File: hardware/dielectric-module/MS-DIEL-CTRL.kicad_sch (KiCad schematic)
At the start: 54 parts, among them J1 24V_IN, J2 CAN, J3 FLUSH_SOL, J4 PUMP_CHILL_DEION, J5 ANALOG_SENSORS, J6 TEMP_1WIRE, J7 FLOW_FLOATS, J8 PROG_USB, Q1 AO3400A, Q2 AO3400A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

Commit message: hw(dielectric): human-readable schematic engine (power glyphs, stubbed labels, blocks, NC, PWR_FLAG, title); add missing MCP2518FD crystal; ERC 0 errors
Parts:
- added C11, C12: 18pF, Capacitor_SMD:C_0805_2012Metric, symbol Device:C
- added Y1: 40MHz, Crystal:Crystal_SMD_3215-2Pin_3.2x1.5mm, symbol Device:Crystal
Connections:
- net GND: now also C11.2, C12.2
- net OSC1: now also C11.1, Y1.1
- net OSC2: now also C12.1, Y1.2
- no-connect marks 0 -> 20
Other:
- note added: "ANALOG + DIGITAL SENSORS"
- note added: "CAN-FD: MCP2518FD + TJA1051 xcvr"
- note added: "ESP32-S3 MCU + PROGRAM / USB HEADER"
- note added: "FLUSH SOLENOID DRIVERS (low-side N-FET)"
- note added: "POWER: 24V in -> 5V buck -> 3V3 LDO"
- note added: "PUMP / CHILLER / DEIONISER (SSR drive)"
- company: (none) -> Microspark
- title: (none) -> MS-DIEL-CTRL  Dielectric / Coolant CAN-FD Controller
- moved on the sheet: C1, C10, C2, C3, C4, C5, C6, C7, C8, C9, D1, D2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

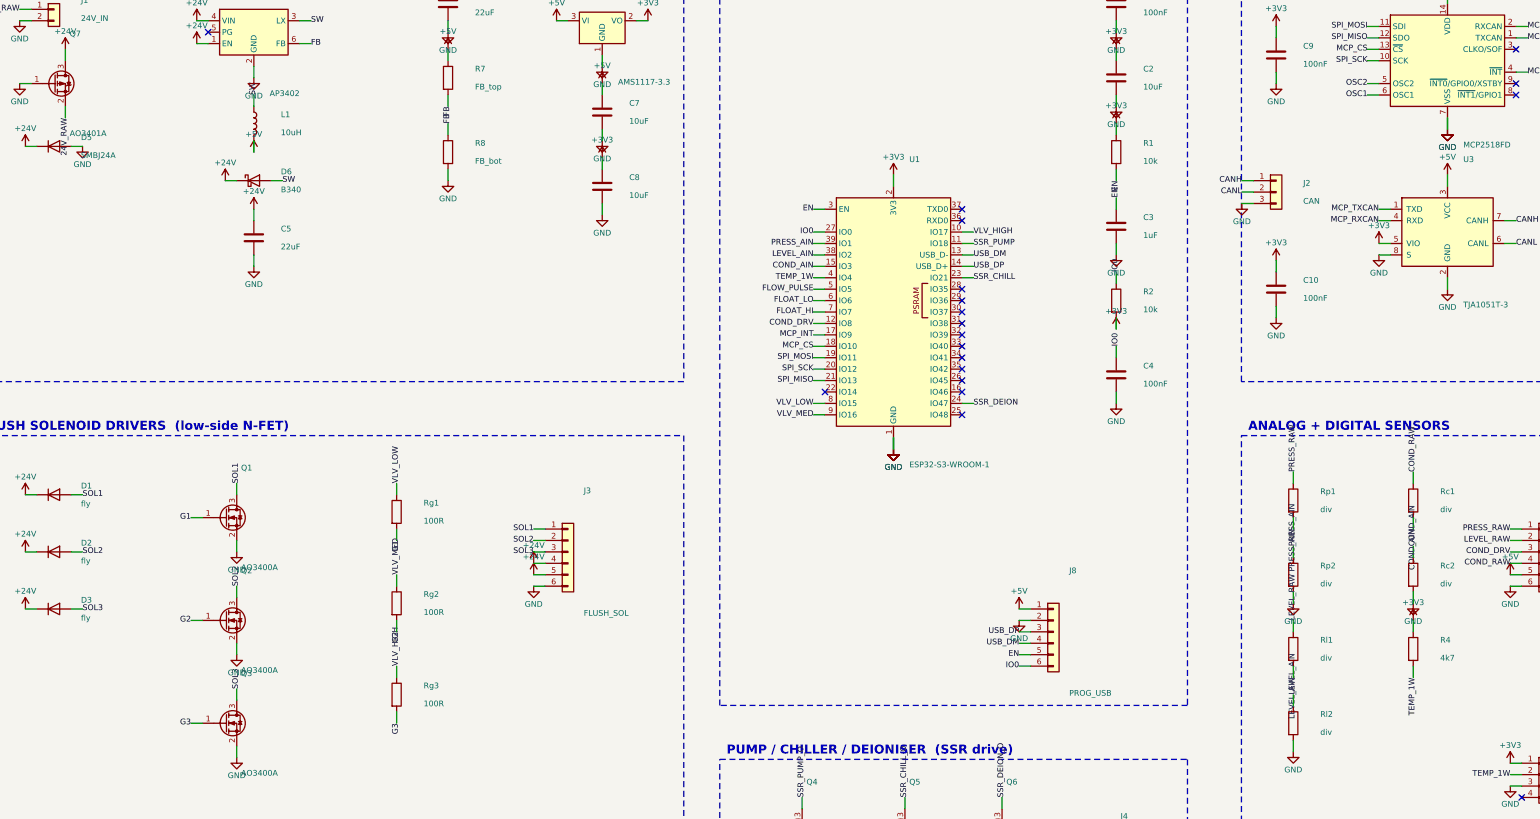
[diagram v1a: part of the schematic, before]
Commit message: hw(dielectric): assign real values to FB divider, sensor dividers, solenoid flyback diodes
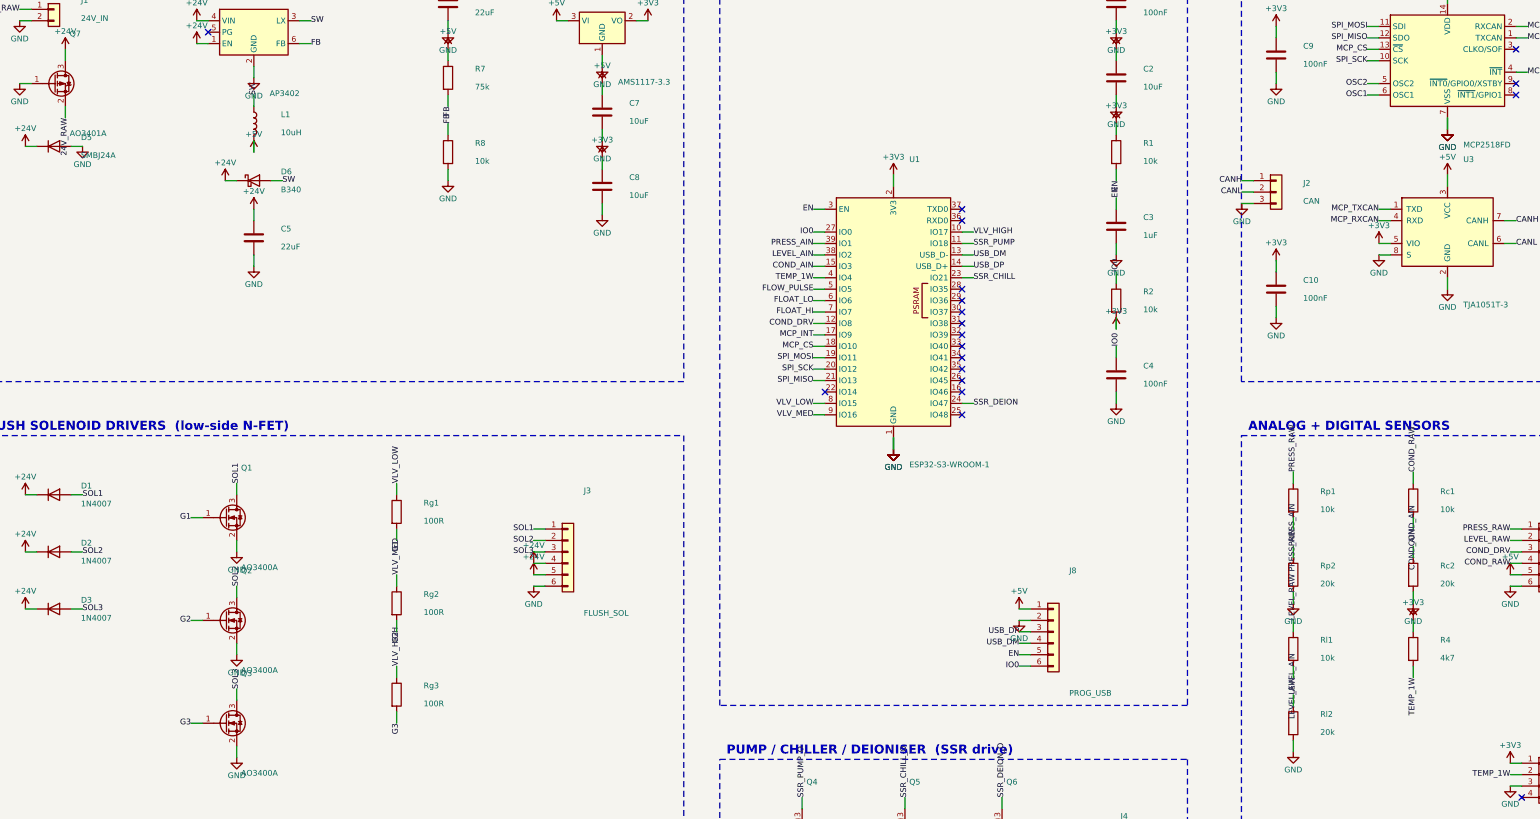
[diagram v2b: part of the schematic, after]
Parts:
- D1, D2, D3: value fly -> 1N4007
- R7: value FB_top -> 75k
- R8: value FB_bot -> 10k
- Rc1, Rl1, Rp1: value div -> 10k
- Rc2, Rl2, Rp2: value div -> 20k
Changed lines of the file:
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@@
 		(property "Reference" "R7" (at 121.57 42.45 0)
 			(effects (font (size 1.27 1.27)) (justify left)))
-		(property "Value" "FB_top" (at 121.57 46.45 0)
+		(property "Value" "75k" (at 121.57 46.45 0)
 			(effects (font (size 1.27 1.27)) (justify left)))
 		(property "Footprint" "Resistor_SMD:R_0805_2012Metric" (at 115.57 44.45 0)
@@
 		(property "Reference" "R8" (at 121.57 58.96 0)
 			(effects (font (size 1.27 1.27)) (justify left)))
-		(property "Value" "FB_bot" (at 121.57 62.96 0)
+		(property "Value" "10k" (at 121.57 62.96 0)
 			(effects (font (size 1.27 1.27)) (justify left)))
 		(property "Footprint" "Resistor_SMD:R_0805_2012Metric" (at 115.57 60.96 0)
@@
 		(property "Reference" "D1" (at 33.94 135.16 0)
 			(effects (font (size 1.27 1.27)) (justify left)))
-		(property "Value" "fly" (at 33.94 139.16 0)
+		(property "Value" "1N4007" (at 33.94 139.16 0)
 			(effects (font (size 1.27 1.27)) (justify left)))
 		(property "Footprint" "Diode_SMD:D_SMA" (at 27.94 137.16 0)
@@
 		(property "Reference" "D2" (at 33.94 147.86 0)
 			(effects (font (size 1.27 1.27)) (justify left)))
-		(property "Value" "fly" (at 33.94 151.86 0)
+		(property "Value" "1N4007" (at 33.94 151.86 0)
 			(effects (font (size 1.27 1.27)) (justify left)))
 		(property "Footprint" "Diode_SMD:D_SMA" (at 27.94 149.86 0)
@@
 		(property "Reference" "D3" (at 33.94 160.56 0)
 			(effects (font (size 1.27 1.27)) (justify left)))
-		(property "Value" "fly" (at 33.94 164.56 0)
+		(property "Value" "1N4007" (at 33.94 164.56 0)
 			(effects (font (size 1.27 1.27)) (justify left)))
 		(property "Footprint" "Diode_SMD:D_SMA" (at 27.94 162.56 0)
@@
 		(property "Reference" "Rp1" (at 309.53 136.43 0)
 			(effects (font (size 1.27 1.27)) (justify left)))
-		(property "Value" "div" (at 309.53 140.43 0)
+		(property "Value" "10k" (at 309.53 140.43 0)
 			(effects (font (size 1.27 1.27)) (justify left)))
 		(property "Footprint" "Resistor_SMD:R_0805_2012Metric" (at 303.53 138.43 0)
@@
 		(property "Reference" "Rp2" (at 309.53 152.94 0)
 			(effects (font (size 1.27 1.27)) (justify left)))
-		(property "Value" "div" (at 309.53 156.94 0)
+		(property "Value" "20k" (at 309.53 156.94 0)
 			(effects (font (size 1.27 1.27)) (justify left)))
 		(property "Footprint" "Resistor_SMD:R_0805_2012Metric" (at 303.53 154.94 0)
@@
 		(property "Reference" "Rl1" (at 309.53 169.45 0)
 			(effects (font (size 1.27 1.27)) (justify left)))
-		(property "Value" "div" (at 309.53 173.45 0)
+		(property "Value" "10k" (at 309.53 173.45 0)
 			(effects (font (size 1.27 1.27)) (justify left)))
 		(property "Footprint" "Resistor_SMD:R_0805_2012Metric" (at 303.53 171.45 0)
@@
 		(property "Reference" "Rl2" (at 309.53 185.96 0)
 			(effects (font (size 1.27 1.27)) (justify left)))
-		(property "Value" "div" (at 309.53 189.96 0)
+		(property "Value" "20k" (at 309.53 189.96 0)
 			(effects (font (size 1.27 1.27)) (justify left)))
 		(property "Footprint" "Resistor_SMD:R_0805_2012Metric" (at 303.53 187.96 0)
@@
 		(property "Reference" "Rc1" (at 336.2 136.43 0)
 			(effects (font (size 1.27 1.27)) (justify left)))
-		(property "Value" "div" (at 336.2 140.43 0)
+		(property "Value" "10k" (at 336.2 140.43 0)
 			(effects (font (size 1.27 1.27)) (justify left)))
 		(property "Footprint" "Resistor_SMD:R_0805_2012Metric" (at 330.2 138.43 0)
@@
 		(property "Reference" "Rc2" (at 336.2 152.94 0)
 			(effects (font (size 1.27 1.27)) (justify left)))
-		(property "Value" "div" (at 336.2 156.94 0)
+		(property "Value" "20k" (at 336.2 156.94 0)
 			(effects (font (size 1.27 1.27)) (justify left)))
 		(property "Footprint" "Resistor_SMD:R_0805_2012Metric" (at 330.2 154.94 0)
